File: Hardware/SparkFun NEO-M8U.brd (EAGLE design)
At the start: 40.6 x 33 mm, 92 parts, among them J13 U.FL, J2 Qwiic Right Angle, J4 Qwiic Right Angle, U1 U-BLOX_NEO-M8T, U2 3.3V

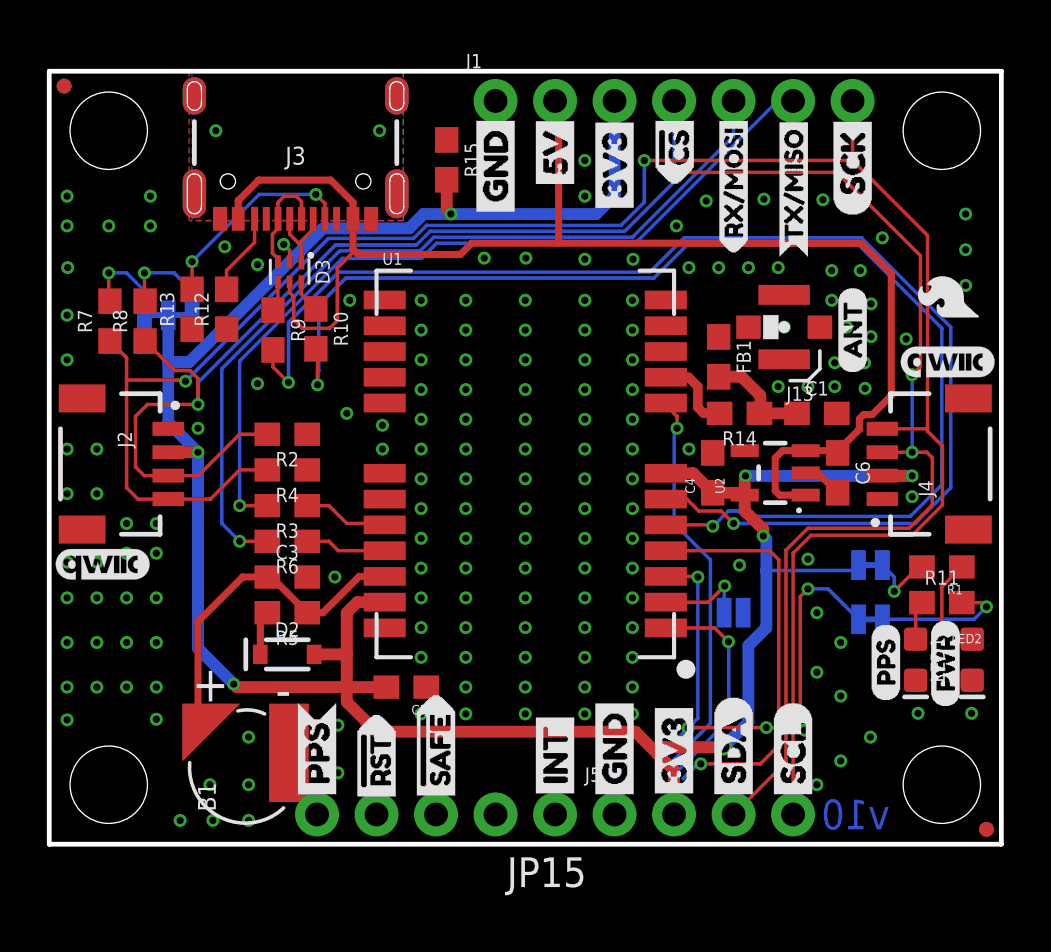
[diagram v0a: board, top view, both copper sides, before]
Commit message: Updates design with the M8U module
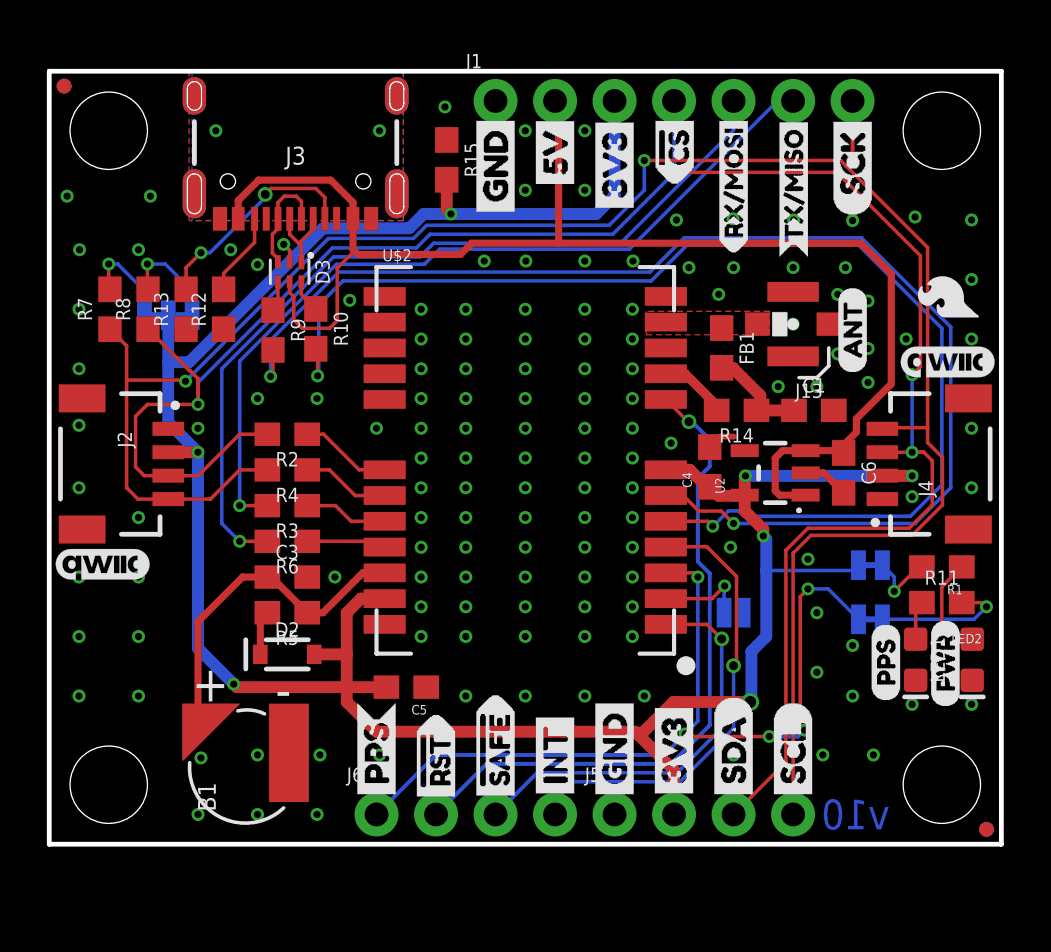
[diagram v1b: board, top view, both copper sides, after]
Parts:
- removed JP15: (no value), SparkFun-Connectors:1X05_NO_SILK
- removed U1: U-BLOX_NEO-M8T, SparkFun-GPS:NEO-M9N/M8T
- added J6: (no value), SparkFun-Connectors:1X04_NO_SILK
- added U$2: U-BLOX_MEO-M8U, SparkFun-GPS:NEO-M9N/M8T/M8U
- moved U$35 2.54 mm to (16.5, 1.40)
- moved U$36 2.54 mm to (16.5, 1.40)
- moved U$43 2.54 mm to (14.0, 1.65)
- moved U$44 2.54 mm to (14.0, 1.65)
- moved U$39 2.54 mm to (19.1, 1.40)
- moved U$40 2.54 mm to (19.1, 1.40)
- moved R8 0.52 mm to (4.22, 22.8)
- moved R7 0.51 mm to (2.59, 22.8)
- moved J13 0.40 mm to (31.8, 22.2)
- moved FB1 0.40 mm to (28.7, 21.2)
- moved LOGO2 0.38 mm to (20.2, 20.3)
- moved U$22 0.38 mm to (24.5, 18.0)
- moved C4 0.28 mm to (28.2, 16.1)
- moved R13 0.25 mm to (5.84, 22.8)
- moved C6 0.25 mm to (33.9, 15.8)
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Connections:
- removed net INT0: JP15.2, U1.4
- removed net INT1: JP15.1, U1.15
- removed net RXLV: R6.1, U1.21
- removed net TXLV: R3.1, U1.20
- new net EXT_INT: J6.4, U$2.4
- new net N$15: R3.1, U$2.20
- new net N$16: R6.1, U$2.21
- net !RESET: now also J6.2, U$2.8; no longer JP15.4, U1.8
- net 3.3V: now also U$2.23, U$2.7; no longer U1.23, U1.7
- net BACKUP: now also U$2.22; no longer U1.22
- net D_SEL: now also U$2.2; no longer U1.2
- net GND: now also U$2.10, U$2.12, U$2.13, U$2.24; no longer U1.10, U1.12, U1.13, U1.24
- net GPS_ANT1: now also U$2.11; no longer U1.11
- net N$11: now also U$2.6; no longer U1.6
- net N$12: now also U$2.5; no longer U1.5
- net N$13: now also U$2.19; no longer U1.19
- net N$3: now also U$2.18; no longer U1.18
- net PPS: now also J6.1, U$2.3; no longer JP15.5, U1.3
- net TP2/!SAFE: now also J6.3, U$2.1; no longer JP15.3, U1.1
- net VCC_RF: now also U$2.9; no longer U1.9
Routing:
- net EXT_INT: track 0.00 -> 19.6 mm, vias 0 -> 1
- net INT0: track 17.6 -> 0.00 mm, vias 1 -> 0
- net PPS: track 23.6 -> 37.2 mm
- net !RESET: track 16.9 -> 28.5 mm
- net TP2/!SAFE: track 9.35 -> 17.6 mm
- net N$3: track 0.00 -> 3.94 mm
- net N$13: track 0.00 -> 3.76 mm
- net TXLV: track 3.65 -> 0.00 mm
- net N$15: track 0.00 -> 3.59 mm
- net RXLV: track 3.47 -> 0.00 mm
- net N$16: track 0.00 -> 3.41 mm
- net GND: track 2.56 -> 4.02 mm, vias 169 -> 141
- net N$12: track 53.5 -> 52.8 mm
- net N$9: track 8.86 -> 9.40 mm
- net VCC_RF: track 3.45 -> 2.94 mm
- added copper zone on layer 1, net GPS_ANT1

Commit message: Updates the ground and shield pour
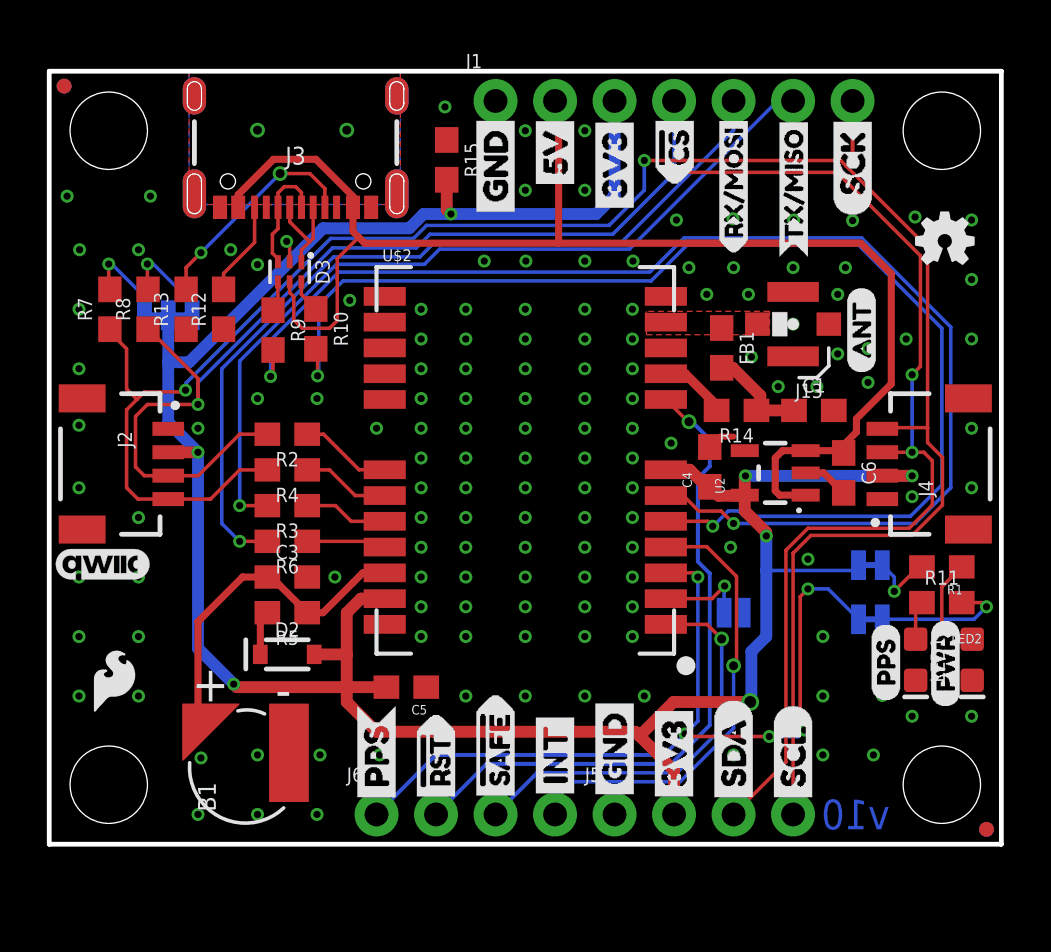
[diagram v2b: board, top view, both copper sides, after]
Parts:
- removed U$13: (no value), SparkFun-Aesthetics:QWIIC_4MM
- moved U$33 39.2 mm to (2.77, 6.99), turned to 0 degrees
- moved LOGO1 35.7 mm to (38.2, 25.8), flipped to the top
- moved U$25 0.38 mm to (34.7, 20.1)
- moved U$1 0.13 mm to (29.2, 1.52)
- moved U$3 0.13 mm to (31.8, 1.52)
- moved U$4 0.13 mm to (29.2, 1.52)
- moved U$43 0.13 mm to (14.0, 1.52)
- moved U$44 0.13 mm to (14.0, 1.52)
- moved U$5 0.13 mm to (31.8, 1.52)
- moved U$6 0.13 mm to (26.7, 1.52)
- moved U$7 0.13 mm to (26.7, 1.52)
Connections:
- net SHLD renamed SHIELD
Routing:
- net USB_D-: track 3.36 -> 4.38 mm
- net SDA/!CS: track 88.2 -> 87.7 mm
- net GND: track 4.02 -> 4.09 mm, vias 141 -> 142

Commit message: Updates design to improve ground pout
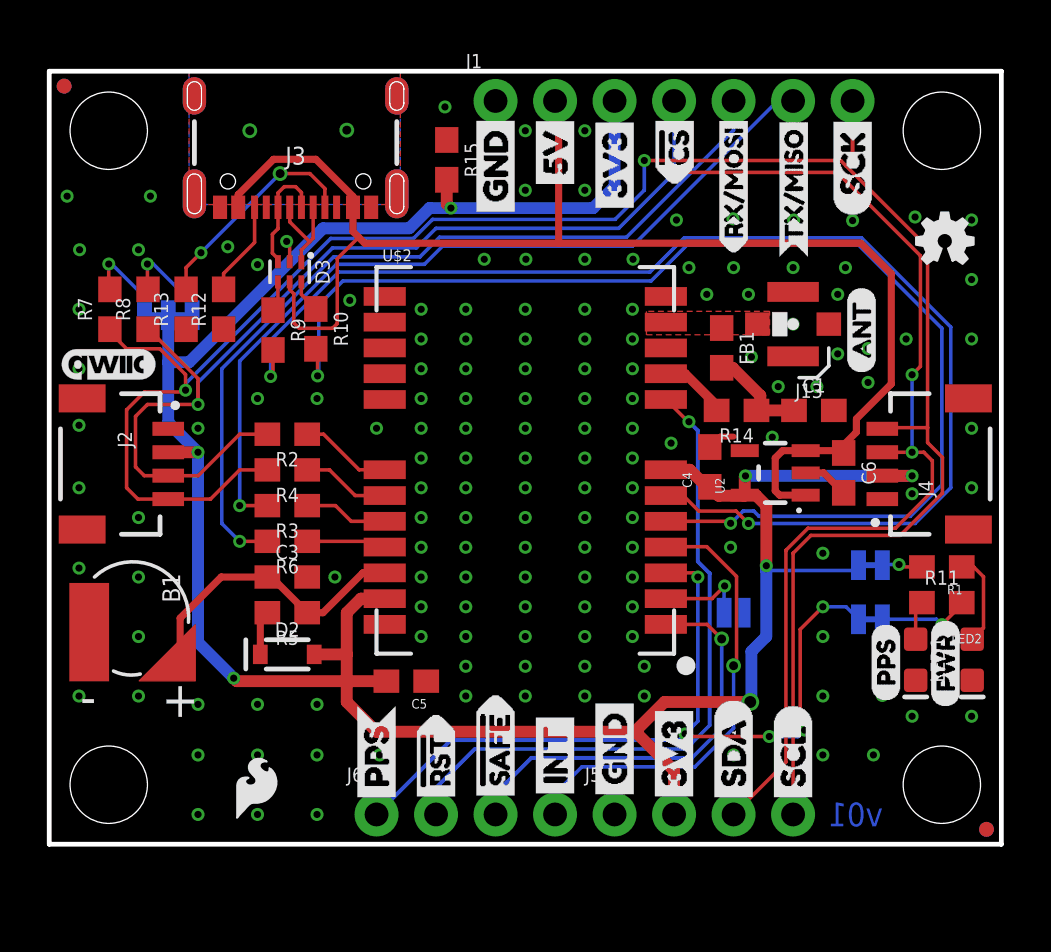
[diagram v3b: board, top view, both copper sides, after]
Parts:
- moved U$14 8.54 mm to (2.54, 20.5)
- moved B1 7.98 mm to (3.56, 9.65), turned to 270 degrees
- moved U$33 7.60 mm to (8.84, 2.41)
- moved C5 0.25 mm to (15.2, 6.96)
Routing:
- net N$4: track 5.79 -> 3.93 mm
- net BACKUP: track 14.3 -> 12.8 mm
- net PPS: track 37.2 -> 35.7 mm
- net N$1: track 2.94 -> 1.74 mm
- net SCL/SCK: track 89.1 -> 90.1 mm
- net TP2/!SAFE: track 17.6 -> 18.1 mm
- net GND: vias 142 -> 149
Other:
- board text added: "v01"
- board text removed: "v10"

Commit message: Adds silk for the orientation of the IMU
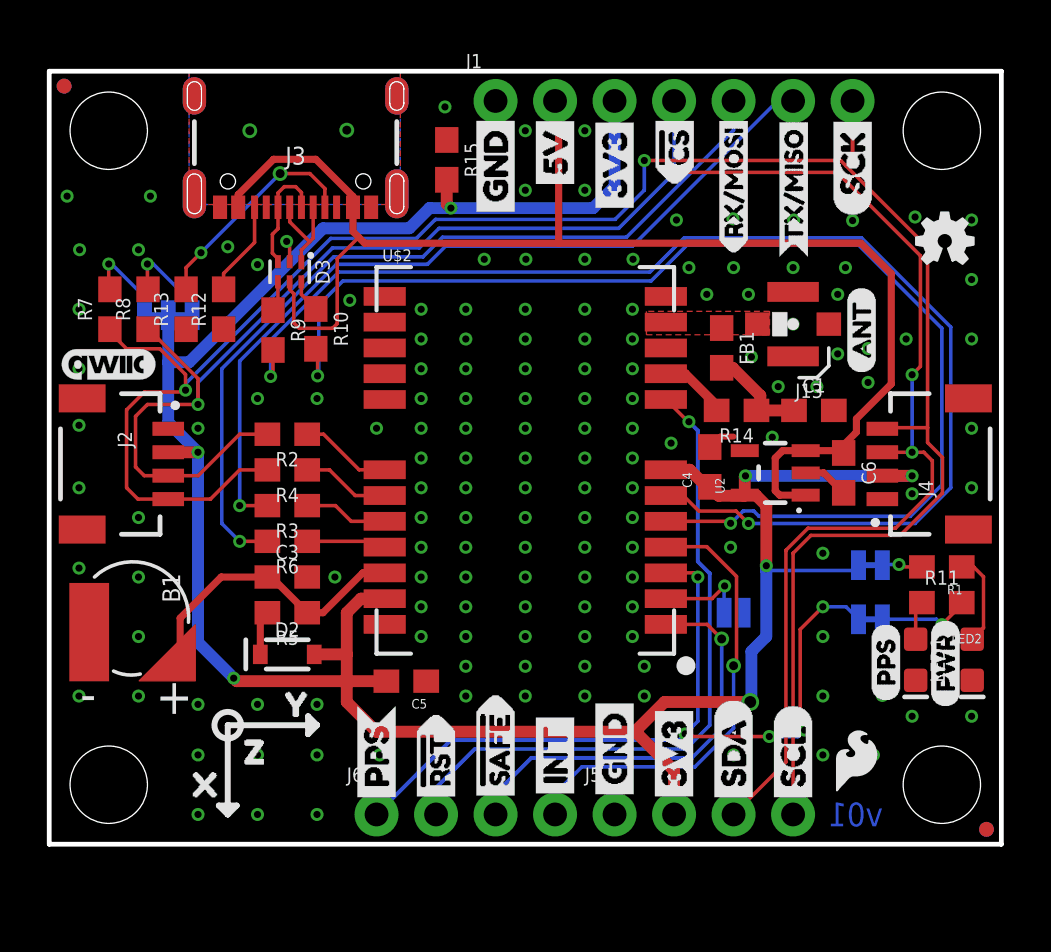
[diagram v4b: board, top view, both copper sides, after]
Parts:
- added U$13: (no value), Orientation:X1
- added U$27: (no value), Orientation:Y2
- added U$28: (no value), Orientation:Z0
- moved U$33 25.6 mm to (34.4, 3.58)
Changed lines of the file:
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@@
 <setting verticaltext="up"/>
 </settings>
-<grid distance="0.05" unitdist="inch" unit="inch" style="lines" multiple="1" display="yes" altdistance="0.001" altunitdist="inch" altunit="inch"/>
+<grid distance="0.05" unitdist="inch" unit="inch" style="lines" multiple="1" display="yes" altdistance="0.005" altunitdist="inch" altunit="inch"/>
 <layers>
 <layer number="1" name="Top" color="4" fill="1" visible="yes" active="yes"/>
@@
 <dimension x1="2.54" y1="30.48" x2="38.1" y2="30.48" x3="20.32" y3="45.72" textsize="1.778" textratio="15" layer="47" unit="inch"/>
 <text x="12.7" y="-17.78" size="1.778" layer="51" font="vector">Elias Santistevan</text>
-<text x="1.3208" y="5.5372" size="1.524" layer="21" font="vector" ratio="15">-</text>
-<text x="4.8006" y="5.4356" size="1.524" layer="21" font="vector" ratio="15">+</text>
+<text x="1.3208" y="5.6642" size="1.524" layer="21" font="vector" ratio="15">-</text>
+<text x="4.5466" y="5.5626" size="1.524" layer="21" font="vector" ratio="15">+</text>
 <rectangle x1="29.21" y1="8.763" x2="30.099" y2="9.144" layer="42"/>
+<wire x1="7.62" y1="1.27" x2="7.62" y2="5.08" width="0.254" layer="21"/>
+<wire x1="7.62" y1="5.08" x2="11.43" y2="5.08" width="0.254" layer="21"/>
+<wire x1="7.62" y1="1.27" x2="7.239" y2="1.651" width="0.254" layer="21"/>
+<wire x1="7.239" y1="1.651" x2="8.001" y2="1.651" width="0.254" layer="21"/>
+<wire x1="8.001" y1="1.651" x2="7.62" y2="1.27" width="0.254" layer="21"/>
+<wire x1="11.43" y1="5.08" x2="11.049" y2="5.461" width="0.254" layer="21"/>
+<wire x1="11.049" y1="5.461" x2="11.049" y2="4.699" width="0.254" layer="21"/>
+<wire x1="11.049" y1="4.699" x2="11.43" y2="5.08" width="0.254" layer="21"/>
+<circle x="7.62" y="5.08" radius="0.567959375" width="0.254" layer="21"/>
 </plain>
 <attributes>
@@
 <element name="U$38" library="Labels" package="SCK-(]-04" value="" x="34.29" y="26.797" smashed="yes" rot="R90"/>
 <element name="U$41" library="Labels" package="SCK-(]-04" value="" x="34.29" y="26.797" smashed="yes" rot="MR90"/>
-<element name="U$33" library="SparkFun-Aesthetics" package="SFE_LOGO_FLAME_.1" value="" x="8.8392" y="2.413" smashed="yes"/>
+<element name="U$33" library="SparkFun-Aesthetics" package="SFE_LOGO_FLAME_.1" value="" x="34.4424" y="3.5814" smashed="yes"/>
 <element name="U$26" library="buzzard_labels (36)" package="RX#MOSI2" value="" x="29.21" y="25.1714" smashed="yes" rot="R90"/>
 <element name="U$31" library="buzzard_labels (36)" package="RX#MOSI3" value="" x="29.2354" y="24.2316" smashed="yes" rot="MR90"/>
@@
 <attribute name="VALUE" x="14.22" y="7.383" size="0.508" layer="27"/>
 </element>
+<element name="U$13" library="Orientation" package="X1" value="" x="5.207" y="2.54" smashed="yes"/>
+<element name="U$27" library="Orientation" package="Y2" value="" x="9.144" y="5.969" smashed="yes"/>
+<element name="U$28" library="Orientation" package="Z0" value="" x="7.366" y="3.937" smashed="yes"/>
 </elements>
 <signals>
@@
 <wire x1="25.4" y1="29.1846" x2="25.4" y2="27.9146" width="0.1524" layer="16"/>
 <via x="25.4" y="29.1846" extent="1-16" drill="0.3048"/>
-<wire x1="12.0142" y1="25.8572" x2="15.5458625" y2="25.8572" width="0.1524" layer="16"/>
+<wire x1="12.0142" y1="25.8572" x2="15.6728625" y2="25.8572" width="0.1524" layer="16"/>
 <wire x1="25.4" y1="29.1846" x2="33.782" y2="29.1846" width="0.1524" layer="1"/>
 <contactref element="J1" pad="7"/>
@@
 <wire x1="2.5908" y1="21.8576" x2="2.5908" y2="21.9846" width="0.1524" layer="1"/>
 <wire x1="25.4" y1="27.9146" x2="24.1554" y2="26.67" width="0.1524" layer="16"/>
-<wire x1="16.3586625" y1="26.67" x2="15.5458625" y2="25.8572" width="0.1524" layer="16"/>
-<wire x1="24.1554" y1="26.67" x2="16.3586625" y2="26.67" width="0.1524" layer="16"/>
+<wire x1="16.4856625" y1="26.67" x2="15.6728625" y2="25.8572" width="0.1524" layer="16"/>
+<wire x1="24.1554" y1="26.67" x2="16.4856625" y2="26.67" width="0.1524" layer="16"/>
 <wire x1="34.29" y1="31.7246" x2="34.29" y2="29.21" width="0.17" layer="1"/>
 <wire x1="34.29" y1="29.21" x2="34.0233" y2="28.9433" width="0.17" layer="1"/>
@@
 <contactref element="R8" pad="1"/>
 <wire x1="26.67" y1="28.6766" x2="26.67" y2="28.6512" width="0.1524" layer="16"/>
-<wire x1="16.51" y1="26.289" x2="24.3078" y2="26.289" width="0.1524" layer="16"/>
+<wire x1="16.637" y1="26.289" x2="24.3078" y2="26.289" width="0.1524" layer="16"/>
 <wire x1="26.67" y1="28.6512" x2="24.3078" y2="26.289" width="0.1524" layer="16"/>
-<wire x1="12.09114375" y1="25.4508" x2="15.6718" y2="25.4508" width="0.1524" layer="16"/>
-<wire x1="15.6718" y1="25.4508" x2="16.51" y2="26.289" width="0.1524" layer="16"/>
+<wire x1="12.09114375" y1="25.4508" x2="15.7988" y2="25.4508" width="0.1524" layer="16"/>
+<wire x1="15.7988" y1="25.4508" x2="16.637" y2="26.289" width="0.1524" layer="16"/>
 <wire x1="6.35" y1="18.7706" x2="6.35" y2="19.87586875" width="0.1524" layer="1"/>
 <wire x1="37.69396875" y1="16.366628125" x2="37.329996875" y2="16.7306" width="0.1524" layer="1"/>
@@
 <contactref element="J1" pad="5"/>
 <wire x1="29.21" y1="30.48" x2="29.21" y2="31.7246" width="0.1524" layer="16"/>
-<wire x1="12.1412" y1="25.0698" x2="15.8242" y2="25.0698" width="0.1524" layer="16"/>
-<wire x1="15.8242" y1="25.0698" x2="16.6624" y2="25.908" width="0.1524" layer="16"/>
-<wire x1="16.6624" y1="25.908" x2="24.638" y2="25.908" width="0.1524" layer="16"/>
+<wire x1="12.1412" y1="25.0698" x2="15.9512" y2="25.0698" width="0.1524" layer="16"/>
+<wire x1="15.9512" y1="25.0698" x2="16.7894" y2="25.908" width="0.1524" layer="16"/>
+<wire x1="16.7894" y1="25.908" x2="24.638" y2="25.908" width="0.1524" layer="16"/>
 <wire x1="24.638" y1="25.908" x2="29.21" y2="30.48" width="0.1524" layer="16"/>
 </signal>
@@
 <wire x1="31.0896" y1="31.7246" x2="24.892" y2="25.527" width="0.1524" layer="16"/>
 <contactref element="J1" pad="6"/>
-<wire x1="12.255128125" y1="24.752671875" x2="16.015071875" y2="24.752671875" width="0.1524" layer="16"/>
-<wire x1="16.015071875" y1="24.752671875" x2="16.7894" y2="25.527" width="0.1524" layer="16"/>
-<wire x1="16.7894" y1="25.527" x2="24.892" y2="25.527" width="0.1524" layer="16"/>
+<wire x1="12.255128125" y1="24.752671875" x2="16.142071875" y2="24.752671875" width="0.1524" layer="16"/>
+<wire x1="16.142071875" y1="24.752671875" x2="16.9164" y2="25.527" width="0.1524" layer="16"/>
+<wire x1="16.9164" y1="25.527" x2="24.892" y2="25.527" width="0.1524" layer="16"/>
 </signal>
 <signal name="SHIELD">
